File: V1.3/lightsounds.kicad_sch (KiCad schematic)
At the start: 30 parts, among them J1 Conn_01x03_Male, J2 Conn_01x03_Female, SW1 SW_DIP_x04, T1 AO3400A, T2 AO3400A, T5 AO3400A, T6 AO3400A

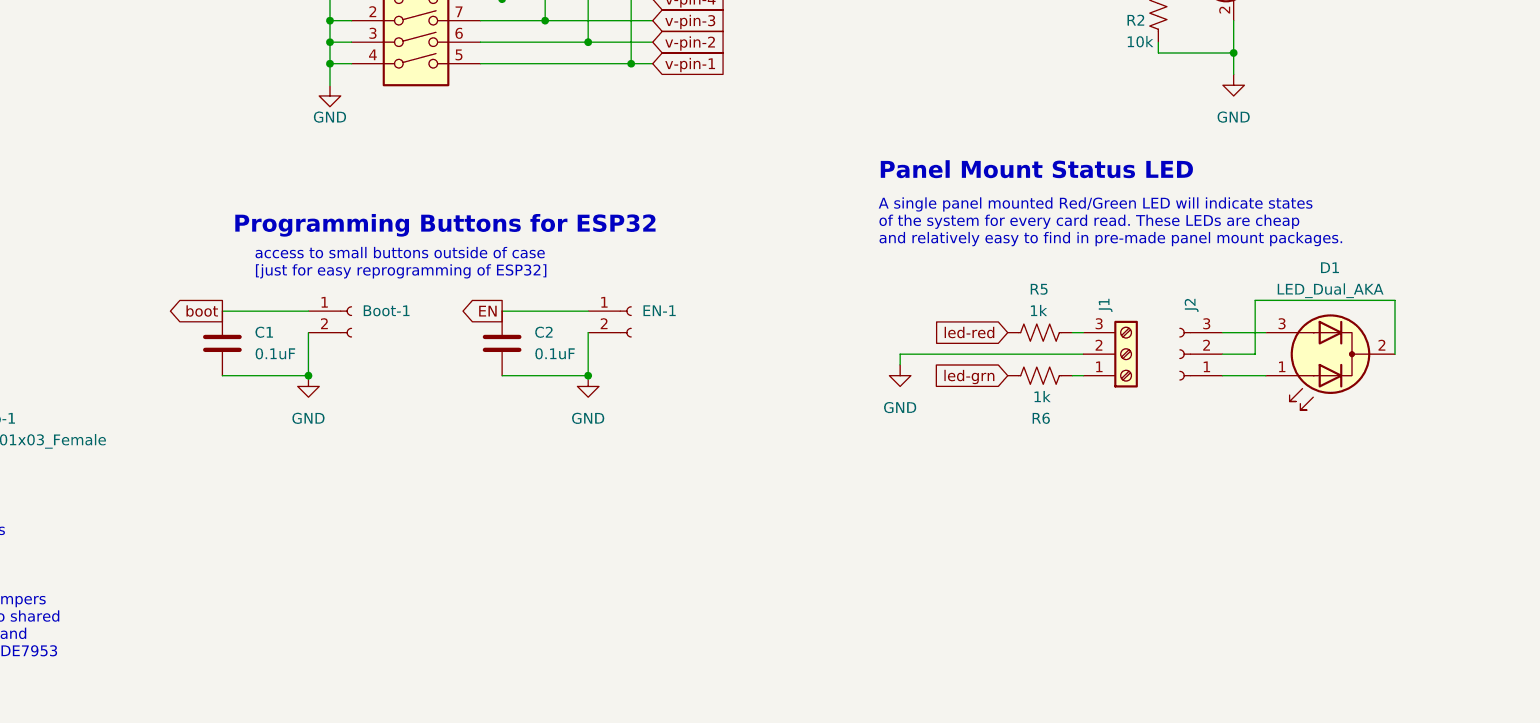
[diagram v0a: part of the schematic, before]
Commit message: clarify door-activator role || Active & Passive door operation
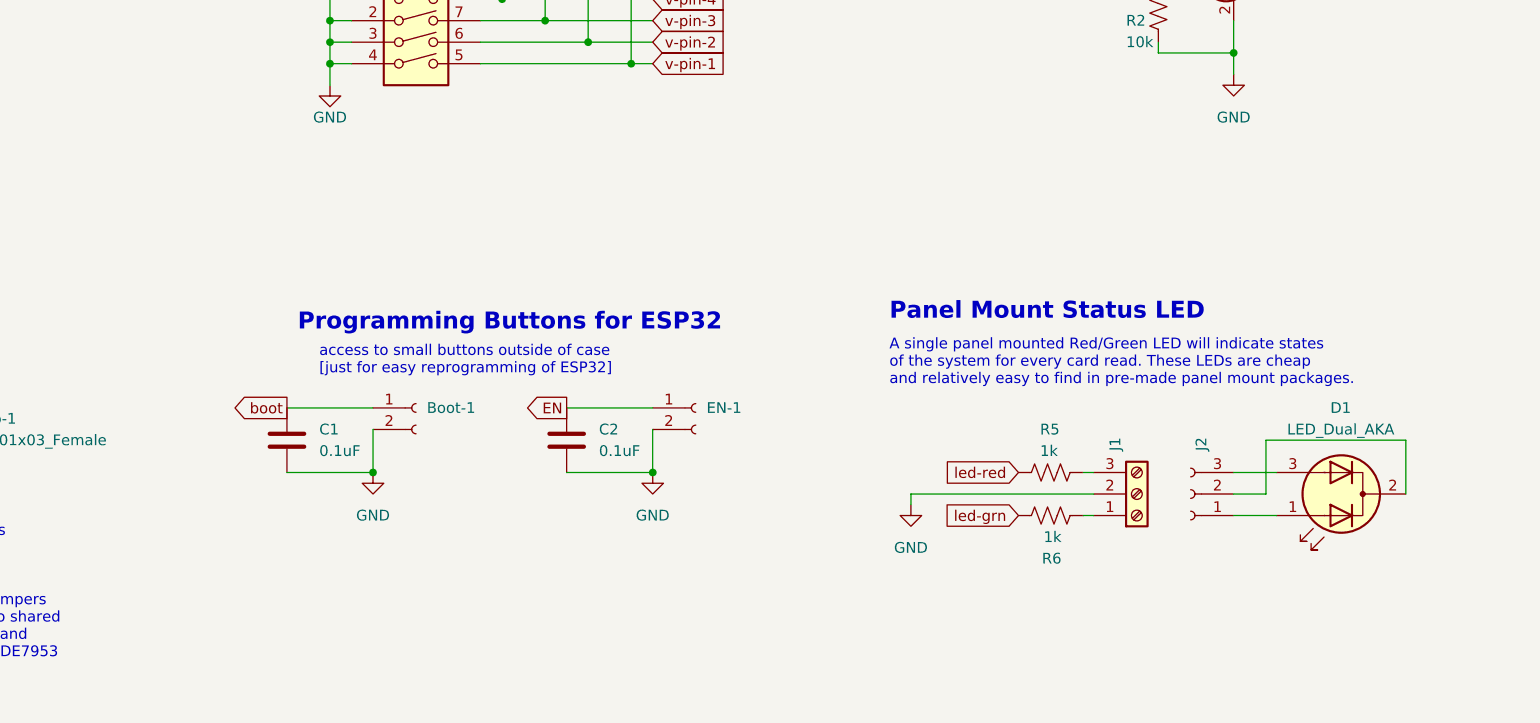
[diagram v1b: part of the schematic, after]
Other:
- moved on the sheet: Boot-1, C1, C2, D1, EN-1, J1, J2, R5, R6
